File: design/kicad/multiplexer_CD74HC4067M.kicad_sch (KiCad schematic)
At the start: 7 parts, among them U2 CD74HC4067M

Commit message: Fix reference labels and update wire connections in MIDI controller and multiplexer schematics
- Adjusted wire connection points in the MIDI controller schematic for better alignment.
- Updated label positions for various components in the MIDI controller schematic.
- Renamed reference designators for capacitors and power connections in the multiplexer schematic to maintain consistency.
- Corrected the reference designators for multiple components to reflect accurate labeling.
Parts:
- renumbered C13 to C11, C14 to C12, D41 to D37, D42 to D38, D43 to D39, D44 to D40, U2 to U1
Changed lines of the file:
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@@
 		(on_board yes)
 		(dnp no)
-		(property "Reference" "C13"
+		(property "Reference" "C11"
 			(at 124.46 147.3199 0)
 			(effects
@@
 			(project "midi_controller"
 				(path "/9e44e663-00d0-4f33-bf1f-c4ad78deb554/3ca90eb8-5cff-4e06-9871-fcb1ae67d879"
-					(reference "C13")
+					(reference "C11")
 					(unit 1)
 				)
@@
 		(dnp no)
 		(fields_autoplaced yes)
-		(property "Reference" "C14"
+		(property "Reference" "C12"
 			(at 138.43 147.3199 0)
 			(effects
@@
 			(project "midi_controller"
 				(path "/9e44e663-00d0-4f33-bf1f-c4ad78deb554/3ca90eb8-5cff-4e06-9871-fcb1ae67d879"
-					(reference "C14")
+					(reference "C12")
 					(unit 1)
 				)
@@
 		(dnp no)
 		(fields_autoplaced yes)
-		(property "Reference" "#PWR04"
+		(property "Reference" "#PWR08"
 			(at 144.78 40.64 0)
 			(effects
@@
 			(project "midi_controller"
 				(path "/9e44e663-00d0-4f33-bf1f-c4ad78deb554/3ca90eb8-5cff-4e06-9871-fcb1ae67d879"
-					(reference "#PWR04")
+					(reference "#PWR08")
 					(unit 1)
 				)
@@
 		(on_board yes)
 		(dnp no)
-		(property "Reference" "D44"
+		(property "Reference" "D40"
 			(at 71.12 167.6399 90)
 			(effects
@@
 			(project "midi_controller"
 				(path "/9e44e663-00d0-4f33-bf1f-c4ad78deb554/3ca90eb8-5cff-4e06-9871-fcb1ae67d879"
-					(reference "D44")
+					(reference "D40")
 					(unit 1)
 				)
@@
 		(dnp no)
 		(fields_autoplaced yes)
-		(property "Reference" "#PWR08"
+		(property "Reference" "#PWR07"
 			(at 129.54 140.97 0)
 			(effects
@@
 			(project "midi_controller"
 				(path "/9e44e663-00d0-4f33-bf1f-c4ad78deb554/3ca90eb8-5cff-4e06-9871-fcb1ae67d879"
-					(reference "#PWR08")
+					(reference "#PWR07")
 					(unit 1)
 				)
@@
 		(on_board yes)
 		(dnp no)
-		(property "Reference" "D42"
+		(property "Reference" "D38"
 			(at 71.12 91.4399 90)
 			(effects
@@
 			(project "midi_controller"
 				(path "/9e44e663-00d0-4f33-bf1f-c4ad78deb554/3ca90eb8-5cff-4e06-9871-fcb1ae67d879"
-					(reference "D42")
+					(reference "D38")
 					(unit 1)
 				)
@@
 		(on_board yes)
 		(dnp no)
-		(property "Reference" "D43"
+		(property "Reference" "D39"
 			(at 71.12 129.5399 90)
 			(effects
@@
 			(project "midi_controller"
 				(path "/9e44e663-00d0-4f33-bf1f-c4ad78deb554/3ca90eb8-5cff-4e06-9871-fcb1ae67d879"
-					(reference "D43")
+					(reference "D39")
 					(unit 1)
 				)
@@
 		(on_board yes)
 		(dnp no)
-		(property "Reference" "D41"
+		(property "Reference" "D37"
 			(at 71.12 53.3399 90)
 			(effects
@@
 			(project "midi_controller"
 				(path "/9e44e663-00d0-4f33-bf1f-c4ad78deb554/3ca90eb8-5cff-4e06-9871-fcb1ae67d879"
-					(reference "D41")
+					(reference "D37")
 					(unit 1)
 				)
@@
 		(on_board yes)
 		(dnp no)
-		(property "Reference" "U2"
+		(property "Reference" "U1"
 			(at 146.9233 41.91 0)
 			(effects
@@
 			(project "midi_controller"
 				(path "/9e44e663-00d0-4f33-bf1f-c4ad78deb554/3ca90eb8-5cff-4e06-9871-fcb1ae67d879"
-					(reference "U2")
+					(reference "U1")
 					(unit 1)
 				)

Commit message: Update capacitor references in multiplexer schematic
Changed capacitor references from C11 to C42 and C12 to C43 in the multiplexer_CD74HC4067M schematic. Updated instances accordingly to maintain consistency in the design.
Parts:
- renumbered C11 to C42, C12 to C43
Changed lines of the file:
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@@
 		(on_board yes)
 		(dnp no)
-		(property "Reference" "C11"
+		(property "Reference" "C42"
 			(at 124.46 147.3199 0)
 			(effects
@@
 			(project "midi_controller"
 				(path "/9e44e663-00d0-4f33-bf1f-c4ad78deb554/3ca90eb8-5cff-4e06-9871-fcb1ae67d879"
-					(reference "C11")
+					(reference "C42")
 					(unit 1)
 				)
@@
 		(dnp no)
 		(fields_autoplaced yes)
-		(property "Reference" "C12"
+		(property "Reference" "C43"
 			(at 138.43 147.3199 0)
 			(effects
@@
 			(project "midi_controller"
 				(path "/9e44e663-00d0-4f33-bf1f-c4ad78deb554/3ca90eb8-5cff-4e06-9871-fcb1ae67d879"
-					(reference "C12")
+					(reference "C43")
 					(unit 1)
 				)

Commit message: Update kicad binary files
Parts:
- renumbered D37 to D36, D38 to D37, D39 to D38, D40 to D39
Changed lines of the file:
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@@
 		(on_board yes)
 		(dnp no)
-		(property "Reference" "D40"
+		(property "Reference" "D39"
 			(at 71.12 167.6399 90)
 			(effects
@@
 			(project "midi_controller"
 				(path "/9e44e663-00d0-4f33-bf1f-c4ad78deb554/3ca90eb8-5cff-4e06-9871-fcb1ae67d879"
-					(reference "D40")
+					(reference "D39")
 					(unit 1)
 				)
@@
 		(on_board yes)
 		(dnp no)
-		(property "Reference" "D38"
+		(property "Reference" "D37"
 			(at 71.12 91.4399 90)
 			(effects
@@
 			(project "midi_controller"
 				(path "/9e44e663-00d0-4f33-bf1f-c4ad78deb554/3ca90eb8-5cff-4e06-9871-fcb1ae67d879"
-					(reference "D38")
+					(reference "D37")
 					(unit 1)
 				)
@@
 		(on_board yes)
 		(dnp no)
-		(property "Reference" "D39"
+		(property "Reference" "D38"
 			(at 71.12 129.5399 90)
 			(effects
@@
 			(project "midi_controller"
 				(path "/9e44e663-00d0-4f33-bf1f-c4ad78deb554/3ca90eb8-5cff-4e06-9871-fcb1ae67d879"
-					(reference "D39")
+					(reference "D38")
 					(unit 1)
 				)
@@
 		(on_board yes)
 		(dnp no)
-		(property "Reference" "D37"
+		(property "Reference" "D36"
 			(at 71.12 53.3399 90)
 			(effects
@@
 			(project "midi_controller"
 				(path "/9e44e663-00d0-4f33-bf1f-c4ad78deb554/3ca90eb8-5cff-4e06-9871-fcb1ae67d879"
-					(reference "D37")
+					(reference "D36")
 					(unit 1)
 				)

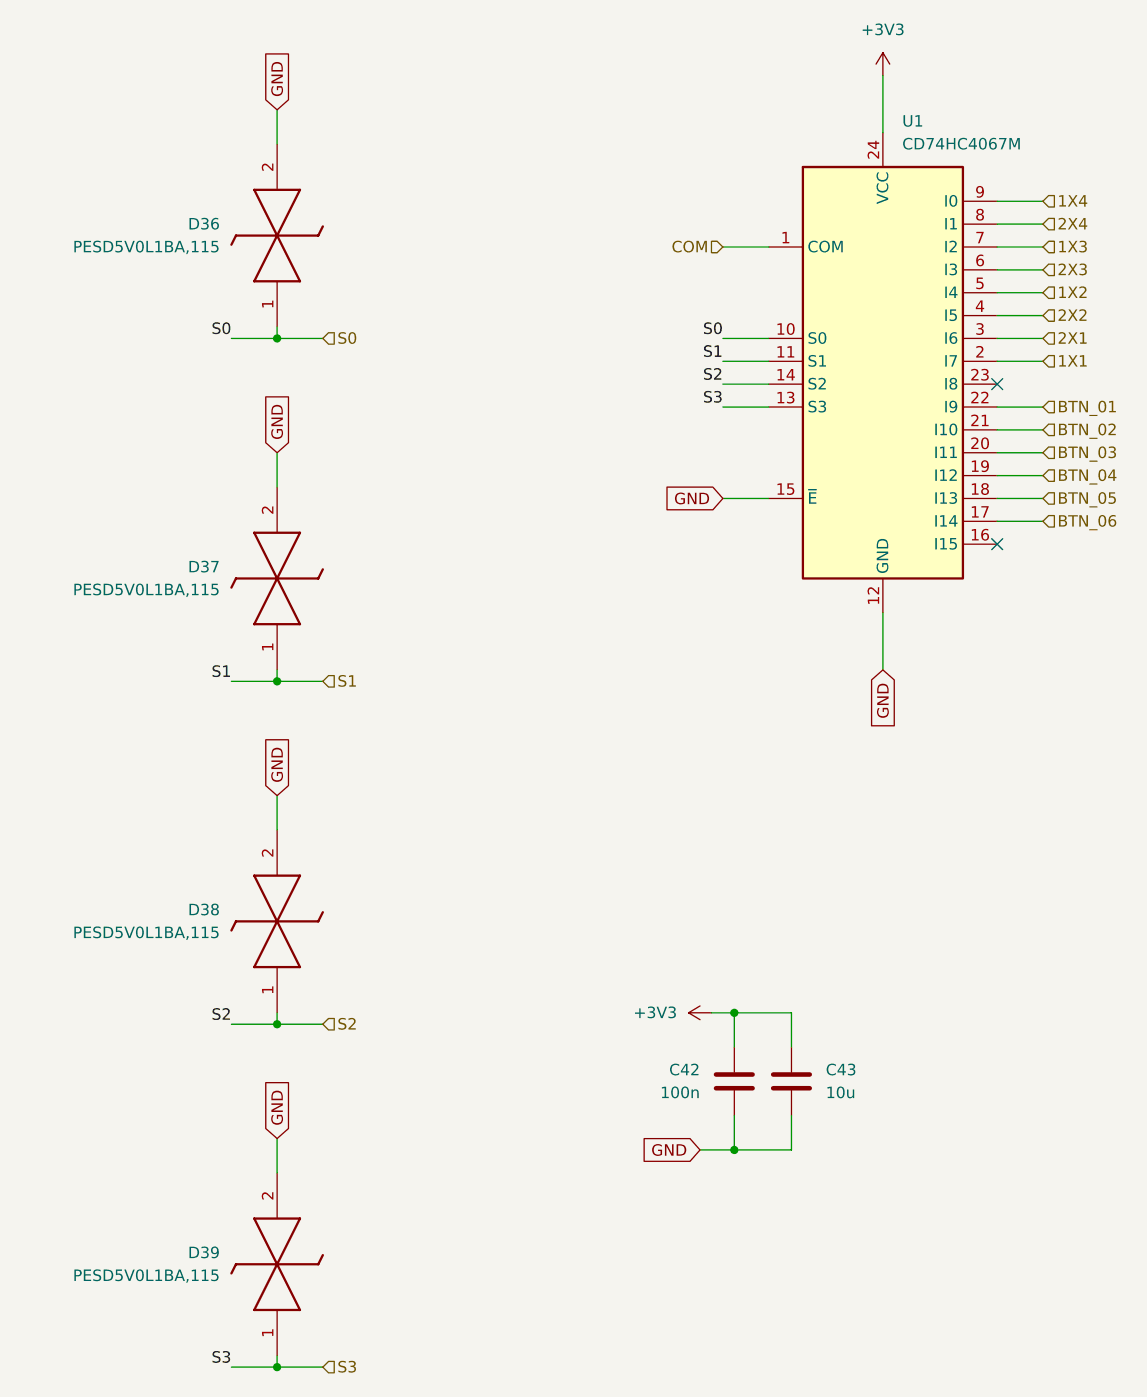
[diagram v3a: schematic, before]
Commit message: Update kicad binary files
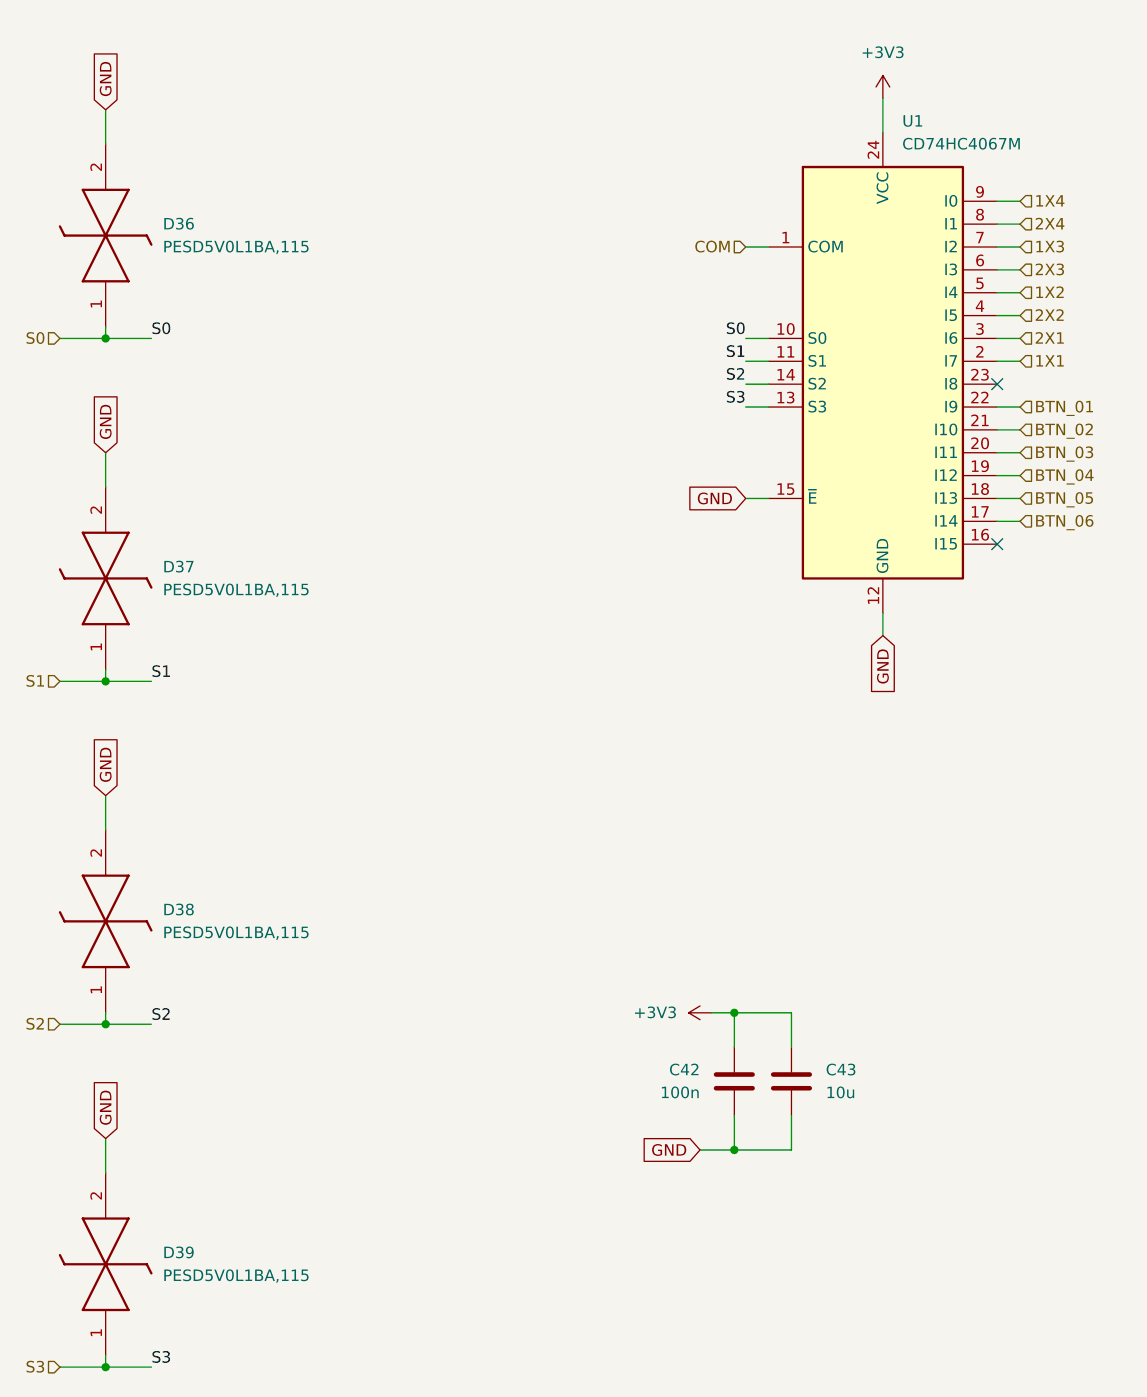
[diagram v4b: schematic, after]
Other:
- moved on the sheet: D36, D37, D38, D39

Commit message: Update kicad binary files
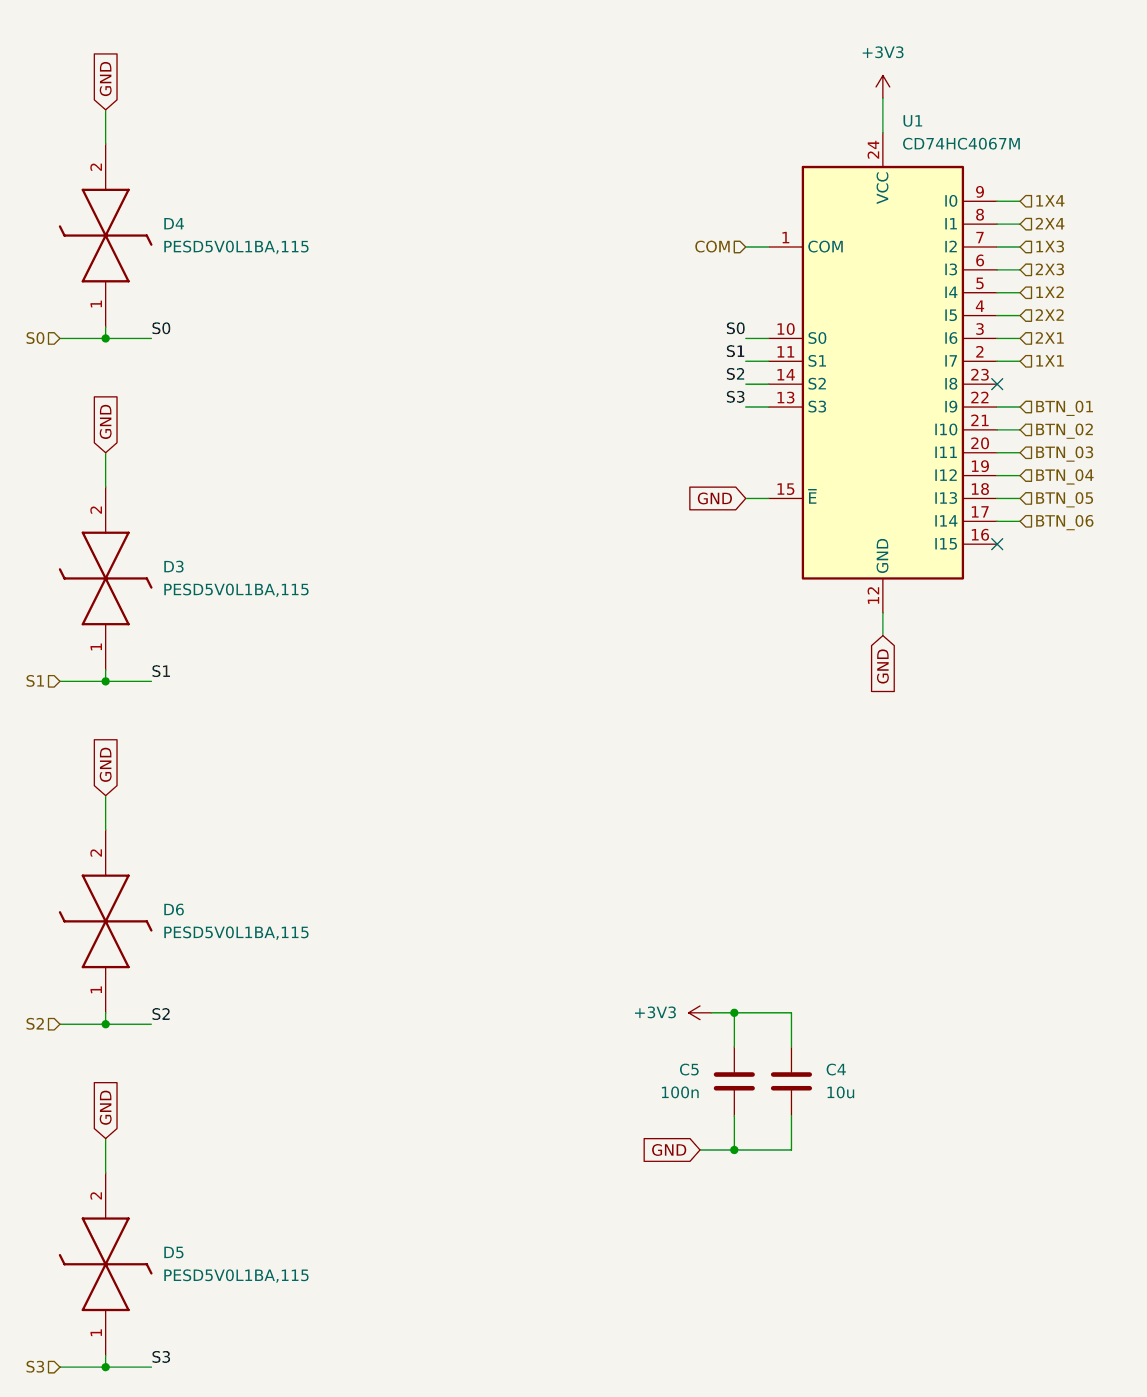
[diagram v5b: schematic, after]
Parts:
- C4: renamed from C43; LCSC (none) -> C1713
- C5: renamed from C42; LCSC (none) -> C1591
- D3: renamed from D37; LCSC (none) -> C85380
- D4: renamed from D36; LCSC (none) -> C85380
- D5: renamed from D39; LCSC (none) -> C85380
- D6: renamed from D38; LCSC (none) -> C85380
- U1: LCSC (none) -> C496123
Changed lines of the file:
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@@
 		(on_board yes)
 		(dnp no)
-		(property "Reference" "C42"
+		(property "Reference" "C5"
 			(at 124.46 147.3199 0)
 			(effects
@@
 		(property "Description" "Unpolarized capacitor"
 			(at 128.27 148.59 0)
+			(effects
+				(font
+					(size 1.27 1.27)
+				)
+				(hide yes)
+			)
+		)
+		(property "LCSC" "C1591"
+			(at 124.46 147.3199 0)
 			(effects
 				(font
@@
 			(project "midi_controller"
 				(path "/9e44e663-00d0-4f33-bf1f-c4ad78deb554/3ca90eb8-5cff-4e06-9871-fcb1ae67d879"
-					(reference "C42")
+					(reference "C5")
 					(unit 1)
 				)
@@
 		(dnp no)
 		(fields_autoplaced yes)
-		(property "Reference" "C43"
+		(property "Reference" "C4"
 			(at 138.43 147.3199 0)
 			(effects
@@
 		(property "Description" "Unpolarized capacitor"
 			(at 134.62 148.59 0)
+			(effects
+				(font
+					(size 1.27 1.27)
+				)
+				(hide yes)
+			)
+		)
+		(property "LCSC" "C1713"
+			(at 138.43 147.3199 0)
 			(effects
 				(font
@@
 			(project "midi_controller"
 				(path "/9e44e663-00d0-4f33-bf1f-c4ad78deb554/3ca90eb8-5cff-4e06-9871-fcb1ae67d879"
-					(reference "C43")
+					(reference "C4")
 					(unit 1)
 				)
@@
 		(on_board yes)
 		(dnp no)
-		(property "Reference" "D39"
+		(property "Reference" "D5"
 			(at 64.77 167.6399 90)
 			(effects
@@
 				)
 				(justify left bottom)
+				(hide yes)
+			)
+		)
+		(property "LCSC" "C85380"
+			(at 64.77 167.6399 0)
+			(effects
+				(font
+					(size 1.27 1.27)
+				)
 				(hide yes)
 			)
@@
 			(project "midi_controller"
 				(path "/9e44e663-00d0-4f33-bf1f-c4ad78deb554/3ca90eb8-5cff-4e06-9871-fcb1ae67d879"
-					(reference "D39")
+					(reference "D5")
 					(unit 1)
 				)
@@
 		(on_board yes)
 		(dnp no)
-		(property "Reference" "D37"
+		(property "Reference" "D3"
 			(at 64.77 91.4399 90)
 			(effects
@@
 				)
 				(justify left bottom)
+				(hide yes)
+			)
+		)
+		(property "LCSC" "C85380"
+			(at 64.77 91.4399 0)
+			(effects
+				(font
+					(size 1.27 1.27)
+				)
 				(hide yes)
 			)
@@
 			(project "midi_controller"
 				(path "/9e44e663-00d0-4f33-bf1f-c4ad78deb554/3ca90eb8-5cff-4e06-9871-fcb1ae67d879"
-					(reference "D37")
+					(reference "D3")
 					(unit 1)
 				)
@@
 		(on_board yes)
 		(dnp no)
-		(property "Reference" "D38"
+		(property "Reference" "D6"
 			(at 64.77 129.5399 90)
 			(effects
@@
 				)
 				(justify left bottom)
+				(hide yes)
+			)
+		)
+		(property "LCSC" "C85380"
+			(at 64.77 129.5399 0)
+			(effects
+				(font
+					(size 1.27 1.27)
+				)
 				(hide yes)
 			)
@@
 			(project "midi_controller"
 				(path "/9e44e663-00d0-4f33-bf1f-c4ad78deb554/3ca90eb8-5cff-4e06-9871-fcb1ae67d879"
-					(reference "D38")
+					(reference "D6")
 					(unit 1)
 				)
@@
 		(on_board yes)
 		(dnp no)
-		(property "Reference" "D36"
+		(property "Reference" "D4"
 			(at 64.77 53.3399 90)
 			(effects
@@
 				)
 				(justify left bottom)
+				(hide yes)
+			)
+		)
+		(property "LCSC" "C85380"
+			(at 64.77 53.3399 0)
+			(effects
+				(font
+					(size 1.27 1.27)
+				)
 				(hide yes)
 			)
@@
 			(project "midi_controller"
 				(path "/9e44e663-00d0-4f33-bf1f-c4ad78deb554/3ca90eb8-5cff-4e06-9871-fcb1ae67d879"
-					(reference "D36")
+					(reference "D4")
 					(unit 1)
 				)
@@
 			(effects
 				(font
+					(size 1.27 1.27)
+				)
+				(hide yes)
+			)
+		)
+		(property "LCSC" "C496123"
+			(at 146.9233 41.91 0)
+			(effects
+				(font
